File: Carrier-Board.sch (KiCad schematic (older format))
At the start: 45 parts, among them J1 CONN_3-6318491-6, J10 Conn_02x03_Odd_Even, J2 Conn_01x0, J3 Conn_02x26_Odd_Even, J4 SI-51009-F, J5 Conn_02x26_Odd_Even, J6 Conn_01x03_Male, J7 Conn_01x03_Male, J8 Conn_01x06_Male, J9 Conn_02x04_Odd_Even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

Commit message: asdf
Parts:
- removed C1, C3: 10uF, Capacitors_SMD:C_0805, symbol CP
- removed C2, C4: 22uF, Capacitors_SMD:C_0805, symbol CP
- removed D5: D_Zener 9V, Diodes_SMD:D_SOD-323, symbol D_Zener
- removed D6, D7, D8: LED, Diodes_SMD:D_1206, symbol LED
- removed J10: Conn_02x03_Odd_Even, Pin_Headers:Pin_Header_Angled_2x03_Pitch2.54mm, symbol Conn_02x03_Odd_Even
- removed J2: Conn_01x0, Connectors:Barrel_Jack_CUI_PJ-036AH-SMT, symbol Barrel_Jack
- removed J4: SI-51009-F, Carrier-Board:SI-51009-F, symbol Conn_02x09_Odd_Even
- removed J6, J7: Conn_01x03_Male, Pin_Headers:Pin_Header_Angled_1x03_Pitch2.54mm, symbol Conn_01x03_Male
- removed J8: Conn_01x06_Male, Pin_Headers:Pin_Header_Angled_1x06_Pitch2.54mm, symbol Conn_01x06_Male
- removed J9: Conn_02x04_Odd_Even, Pin_Headers:Pin_Header_Angled_2x04_Pitch2.54mm, symbol Conn_02x04_Odd_Even
- removed R1, R5: 160k, Resistors_SMD:R_0805, symbol R
- removed R10, R9: 330, Resistors_SMD:R_0805, symbol R
- removed R11, R12, R13: 10K, Resistors_SMD:R_0603, symbol R
- removed R2: 30.1k, Resistors_SMD:R_0805, symbol R
- removed R23: 330, Resistors_SMD:R_0603, symbol R
- removed R24: 180, Resistors_SMD:R_0603, symbol R
- removed R25: 1k, Resistors_SMD:R_0603, symbol R
- removed R3, R7: 100k, Resistors_SMD:R_0805, symbol R
- removed R4: 63.4k, Resistors_SMD:R_0805, symbol R
- removed R6: 51k, Resistors_SMD:R_0805, symbol R
- removed R8: 56k, Resistors_SMD:R_0805, symbol R
- removed SW1, SW2, SW3: SW_Push, Buttons_Switches_SMD:SW_SPST_B3U-1000P, symbol SW_Push
- removed U1, U2: MPM3620, BusSimulator:QFN-20, symbol MPM3620
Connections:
- net labels removed: +12V, +5V, GNDA, PCE3895CT-ND, PCE3900CT-ND, SPI_POWER
- wire segments 102 -> 24
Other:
- note removed: "12V\n"
- note removed: "3V3\n"
- note removed: "5V SBY\n"
- note removed: "Break out\n"
- note removed: "Ethernet"
- note removed: "GPIO\n"
- note removed: "I2C\n"
- note removed: "LED Indicators\n"
- note removed: "MISC SHIT"
- note removed: "Rs232\n"
- note removed: "SPI\n"
- note removed: "Voltage Supply"

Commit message: stuff
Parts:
- added J2: 0532610671, MOLEX_0532610671, symbol 0532610671
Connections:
- new net: J2.S1 (SHIELD), J2.S2 (SHIELD)
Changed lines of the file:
@@
 LIBS:Carrier-Board
 LIBS:SI-51009-F
+LIBS:0532610271
+LIBS:0532610371
+LIBS:0532610471
+LIBS:0532610671
 LIBS:Carrier-Board-cache
 EELAYER 25 0
@@
 +3.3V
 $Comp
-L GNDREF #PWR022
+L GNDREF #PWR8
 U 1 1 5A0C1B77
 P 3700 8250
-F 0 "#PWR022" H 3700 8000 50  0001 C CNN
+F 0 "#PWR8" H 3700 8000 50  0001 C CNN
 F 1 "GNDREF" H 3700 8100 50  0000 C CNN
 F 2 "" H 3700 8250 50  0001 C CNN
@@
 $EndComp
 $Comp
-L GNDREF #PWR023
+L GNDREF #PWR9
 U 1 1 5A0C1C29
 P 3900 10650
-F 0 "#PWR023" H 3900 10400 50  0001 C CNN
+F 0 "#PWR9" H 3900 10400 50  0001 C CNN
 F 1 "GNDREF" H 3900 10500 50  0000 C CNN
 F 2 "" H 3900 10650 50  0001 C CNN
@@
 $EndComp
 $Comp
-L GNDREF #PWR024
+L GNDREF #PWR12
 U 1 1 5A0C1CDB
 P 4000 9450
-F 0 "#PWR024" H 4000 9200 50  0001 C CNN
+F 0 "#PWR12" H 4000 9200 50  0001 C CNN
 F 1 "GNDREF" H 4000 9300 50  0000 C CNN
 F 2 "" H 4000 9450 50  0001 C CNN
@@
 $EndComp
 $Comp
-L GNDREF #PWR025
+L GNDREF #PWR11
 U 1 1 5A0C1D8D
 P 4000 9050
-F 0 "#PWR025" H 4000 8800 50  0001 C CNN
+F 0 "#PWR11" H 4000 8800 50  0001 C CNN
 F 1 "GNDREF" H 4000 8900 50  0000 C CNN
 F 2 "" H 4000 9050 50  0001 C CNN
@@
 $EndComp
 $Comp
-L GNDREF #PWR026
+L GNDREF #PWR10
 U 1 1 5A0C1E3F
 P 4000 8750
-F 0 "#PWR026" H 4000 8500 50  0001 C CNN
+F 0 "#PWR10" H 4000 8500 50  0001 C CNN
 F 1 "GNDREF" H 4000 8600 50  0000 C CNN
 F 2 "" H 4000 8750 50  0001 C CNN
@@
 $EndComp
 $Comp
-L GNDREF #PWR027
+L GNDREF #PWR13
 U 1 1 5A0C1EF1
 P 4000 9850
-F 0 "#PWR027" H 4000 9600 50  0001 C CNN
+F 0 "#PWR13" H 4000 9600 50  0001 C CNN
 F 1 "GNDREF" H 4000 9700 50  0000 C CNN
 F 2 "" H 4000 9850 50  0001 C CNN
@@
 SATA0_RX-
 $Comp
-L GNDREF #PWR028
+L GNDREF #PWR6
 U 1 1 5A0C49FB
 P 1800 10400
-F 0 "#PWR028" H 1800 10150 50  0001 C CNN
+F 0 "#PWR6" H 1800 10150 50  0001 C CNN
 F 1 "GNDREF" H 1800 10250 50  0000 C CNN
 F 2 "" H 1800 10400 50  0001 C CNN
@@
 $EndComp
 $Comp
-L GNDREF #PWR029
+L GNDREF #PWR7
 U 1 1 5A0C4BAB
 P 1900 10050
-F 0 "#PWR029" H 1900 9800 50  0001 C CNN
+F 0 "#PWR7" H 1900 9800 50  0001 C CNN
 F 1 "GNDREF" H 1900 9900 50  0000 C CNN
 F 2 "" H 1900 10050 50  0001 C CNN
@@
 Sata Connector\n
 $Comp
-L GNDREF #PWR030
+L GNDREF #PWR3
 U 1 1 5A0C6A3D
 P 1450 8950
-F 0 "#PWR030" H 1450 8700 50  0001 C CNN
+F 0 "#PWR3" H 1450 8700 50  0001 C CNN
 F 1 "GNDREF" H 1450 8800 50  0000 C CNN
 F 2 "" H 1450 8950 50  0001 C CNN
@@
 $EndComp
 $Comp
-L GNDREF #PWR031
+L GNDREF #PWR4
 U 1 1 5A0C6D48
 P 1500 9350
-F 0 "#PWR031" H 1500 9100 50  0001 C CNN
+F 0 "#PWR4" H 1500 9100 50  0001 C CNN
 F 1 "GNDREF" H 1500 9200 50  0000 C CNN
 F 2 "" H 1500 9350 50  0001 C CNN
@@
 $EndComp
 $Comp
-L GNDREF #PWR032
+L GNDREF #PWR5
 U 1 1 5A0C77C7
 P 1600 8450
-F 0 "#PWR032" H 1600 8200 50  0001 C CNN
+F 0 "#PWR5" H 1600 8200 50  0001 C CNN
 F 1 "GNDREF" H 1600 8300 50  0000 C CNN
 F 2 "" H 1600 8450 50  0001 C CNN
@@
 $EndComp
 $Comp
-L GNDREF #PWR033
+L GNDREF #PWR1
 U 1 1 5A0DCFAA
 P 750 8350
-F 0 "#PWR033" H 750 8100 50  0001 C CNN
+F 0 "#PWR1" H 750 8100 50  0001 C CNN
 F 1 "GNDREF" H 750 8200 50  0000 C CNN
 F 2 "" H 750 8350 50  0001 C CNN
@@
 $EndComp
 $Comp
-L GNDREF #PWR034
+L GNDREF #PWR2
 U 1 1 5A0DD07C
 P 1100 9050
-F 0 "#PWR034" H 1100 8800 50  0001 C CNN
+F 0 "#PWR2" H 1100 8800 50  0001 C CNN
 F 1 "GNDREF" H 1100 8900 50  0000 C CNN
 F 2 "" H 1100 9050 50  0001 C CNN
@@
 $EndComp
 $Comp
-L GNDREF #PWR035
+L GNDREF #PWR14
 U 1 1 5A0DDC34
 P 4500 8450
-F 0 "#PWR035" H 4500 8200 50  0001 C CNN
+F 0 "#PWR14" H 4500 8200 50  0001 C CNN
 F 1 "GNDREF" H 4500 8300 50  0000 C CNN
 F 2 "" H 4500 8450 50  0001 C CNN
@@
 Wire Bus Line
 	16100 3900 4700 3900
+$Comp
+L 0532610671 J2
+U 1 1 5AB9DE55
+P 2450 1900
+F 0 "J2" H 2250 2331 50  0000 L BNN
+F 1 "0532610671" H 2249 1298 50  0000 L BNN
+F 2 "MOLEX_0532610671" H 2450 1900 50  0001 L BNN
+F 3 "None" H 2450 1900 50  0001 L BNN
+F 4 "Good" H 2450 1900 50  0001 L BNN "Field4"
+F 5 "0532610671" H 2450 1900 50  0001 L BNN "Field5"
+F 6 "1.25mm (.049) Pitch PicoBlade Header, Surface Mount, Right Angle, Lead-free, 6 Circuits" H 2450 1900 50  0001 L BNN "Field6"
+F 7 "0.82 USD" H 2450 1900 50  0001 L BNN "Field7"
+F 8 "Molex" H 2450 1900 50  0001 L BNN "Field8"
+	1    2450 1900
+	1    0    0    -1
+$EndComp
 $EndSCHEMATC

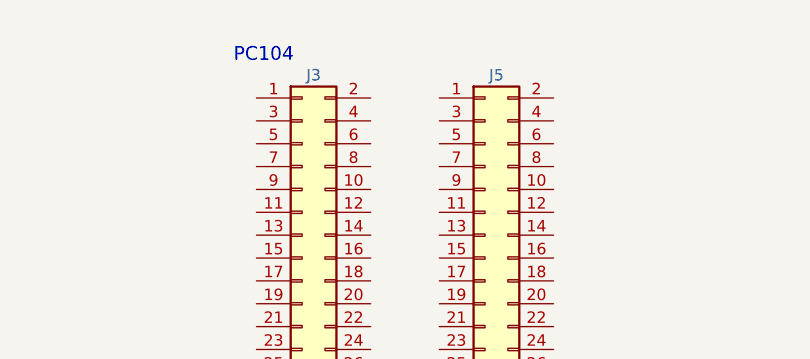
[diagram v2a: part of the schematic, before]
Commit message: Update mCOM connector, correct header refs/silk
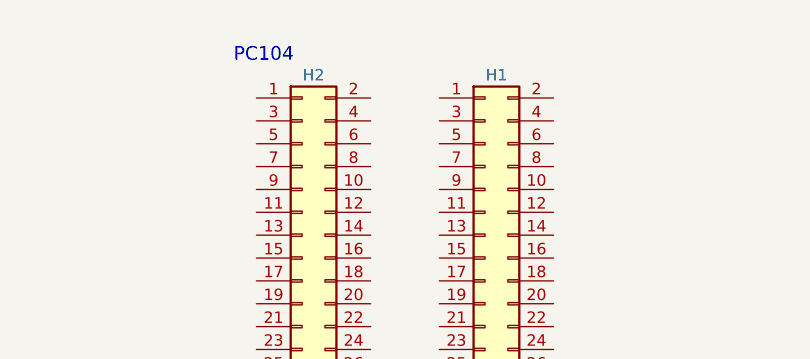
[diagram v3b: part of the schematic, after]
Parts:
- renumbered J5 to H1, J3 to H2
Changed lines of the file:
@@
 LIBS:Carrier-Board
 LIBS:SI-51009-F
+LIBS:MCP6H04-E
+LIBS:BusSimulator
 LIBS:0532610271
 LIBS:0532610371
@@
 $EndComp
 $Comp
-L Conn_02x26_Odd_Even J3
+L Conn_02x26_Odd_Even H2
 U 1 1 5A6C2591
 P 11900 2050
-F 0 "J3" H 11950 3350 50  0000 C CNN
+F 0 "H2" H 11950 3350 50  0000 C CNN
 F 1 "Conn_02x26_Odd_Even" H 11950 650 50  0000 C CNN
 F 2 "Carrier-Board:ESQ-126-XX-X-D" H 11900 2050 50  0001 C CNN
@@
 $EndComp
 $Comp
-L Conn_02x26_Odd_Even J5
+L Conn_02x26_Odd_Even H1
 U 1 1 5A6C25B0
 P 12700 2050
-F 0 "J5" H 12750 3350 50  0000 C CNN
+F 0 "H1" H 12750 3350 50  0000 C CNN
 F 1 "Conn_02x26_Odd_Even" H 12750 650 50  0000 C CNN
 F 2 "Carrier-Board:ESQ-126-XX-X-D" H 12700 2050 50  0001 C CNN

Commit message: SF
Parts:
- H1: value Conn_02x26_Odd_Even -> H1
- H2: value Conn_02x26_Odd_Even -> H2
- J1: value CONN_3-6318491-6 -> s
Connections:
- net CAN_L: now reaches H1.1 (Pin_1)
- net * GPIO PH11: now reaches H1.10 (Pin_10)
- net * ADC1_IN4 (PC4): now reaches H1.13 (Pin_13)
- net * ADC1_IN8 (PC5): now reaches H1.14 (Pin_14)
- net * ADC1_IN5 (PB1): now reaches H1.15 (Pin_15)
- net * ADC1_IN9 (PB0): now reaches H1.16 (Pin_16)
- net * UHF radio UART2_RX / ** UART2_TX: now reaches H1.17 (Pin_17)
- net * UHF radio UART2_TX / ** UART2_RX: now reaches H1.18 (Pin_18)
- net GPS_PPS signal output: now reaches H1.2 (Pin_2)
- net CAN_H: now reaches H1.3 (Pin_3)
- net * I2C3_SDA: now reaches H1.41 (Pin_41)
- net * I2C3_SCL: now reaches H1.43 (Pin_43)
- net 5 V Reaction wheels power supply (default option): now reaches H1.47 (Pin_47)
- net 3.3 V 3C2 board power supply (default option): now reaches H1.48 (Pin_48)
- net *GPIO_PA10: now reaches H1.5 (Pin_5)
- net 3.3V UHF radio power supply (** option 2): now reaches H1.50 (Pin_50)
- net * GPIO_PH6: now reaches H1.7 (Pin_7)
- net * GPIO_PH9: now reaches H1.8 (Pin_8)
- net * GPIO PH10: now reaches H1.9 (Pin_9)
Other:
- note added: "Verify_P10\n"
- moved on the sheet: H1, H2
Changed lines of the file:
@@
 LIBS:Carrier-Board
 LIBS:SI-51009-F
-LIBS:MCP6H04-E
-LIBS:BusSimulator
 LIBS:0532610271
 LIBS:0532610371
@@
 P 9450 4850
 F 0 "J1" H 9800 5100 60  0000 C CNN
-F 1 "CONN_3-6318491-6" H 9800 5450 60  0000 C CNN
+F 1 "CONN_3-6318491-6" H 9800 5450 60  0001 C CNN
 F 2 "BusSimulator:ComExpressMini10" H 9850 2590 60  0001 C CNN
 F 3 "" H 9450 4850 60  0000 C CNN
@@
 P 10950 4850
 F 0 "J1" H 11300 5100 60  0000 C CNN
-F 1 "CONN_3-6318491-6" H 11050 6150 60  0000 C CNN
+F 1 "CONN_3-6318491-6" H 11050 6150 60  0001 C CNN
 F 2 "BusSimulator:ComExpressMini10" H 11350 2590 60  0001 C CNN
 F 3 "" H 10950 4850 60  0000 C CNN
@@
 P 12450 4850
 F 0 "J1" H 12800 5100 60  0000 C CNN
-F 1 "CONN_3-6318491-6" H 13050 6300 60  0000 C CNN
+F 1 "s" H 13050 6300 60  0001 C CNN
 F 2 "BusSimulator:ComExpressMini10" H 12850 2590 60  0001 C CNN
 F 3 "" H 12450 4850 60  0000 C CNN
@@
 P 13950 4850
 F 0 "J1" H 14300 5100 60  0000 C CNN
-F 1 "CONN_3-6318491-6" H 14250 5850 60  0000 C CNN
+F 1 "CONN_3-6318491-6" H 14250 5850 60  0001 C CNN
 F 2 "BusSimulator:ComExpressMini10" H 14350 2590 60  0001 C CNN
 F 3 "" H 13950 4850 60  0000 C CNN
@@
 P 15450 4850
 F 0 "J1" H 15800 5100 60  0000 C CNN
-F 1 "CONN_3-6318491-6" H 15750 5300 60  0000 C CNN
+F 1 "CONN_3-6318491-6" H 15750 5300 60  0001 C CNN
 F 2 "BusSimulator:ComExpressMini10" H 15850 2590 60  0001 C CNN
 F 3 "" H 15450 4850 60  0000 C CNN
@@
 L Conn_02x26_Odd_Even H2
 U 1 1 5A6C2591
-P 11900 2050
-F 0 "H2" H 11950 3350 50  0000 C CNN
-F 1 "Conn_02x26_Odd_Even" H 11950 650 50  0000 C CNN
-F 2 "Carrier-Board:ESQ-126-XX-X-D" H 11900 2050 50  0001 C CNN
-F 3 "" H 11900 2050 50  0001 C CNN
-	1    11900 2050
+P 10200 1850
+F 0 "H2" H 10250 3150 50  0000 C CNN
+F 1 "H2" H 10250 450 50  0000 C CNN
+F 2 "Carrier-Board:ESQ-126-XX-X-D" H 10200 1850 50  0001 C CNN
+F 3 "" H 10200 1850 50  0001 C CNN
+	1    10200 1850
 	1    0    0    -1
 $EndComp
@@
 L Conn_02x26_Odd_Even H1
 U 1 1 5A6C25B0
-P 12700 2050
-F 0 "H1" H 12750 3350 50  0000 C CNN
-F 1 "Conn_02x26_Odd_Even" H 12750 650 50  0000 C CNN
-F 2 "Carrier-Board:ESQ-126-XX-X-D" H 12700 2050 50  0001 C CNN
-F 3 "" H 12700 2050 50  0001 C CNN
-	1    12700 2050
+P 13400 2000
+F 0 "H1" H 13450 3300 50  0000 C CNN
+F 1 "H1" H 13450 600 50  0000 C CNN
+F 2 "Carrier-Board:ESQ-126-XX-X-D" H 13400 2000 50  0001 C CNN
+F 3 "" H 13400 2000 50  0001 C CNN
+	1    13400 2000
 	1    0    0    -1
 $EndComp
@@
 	1    0    0    -1
 $EndComp
+Text GLabel 13200 800  0    60   Input ~ 0
+CAN_L
+Text GLabel 13700 800  2    60   Input ~ 0
+GPS_PPS signal output
+Text GLabel 13200 900  0    60   Input ~ 0
+CAN_H
+Text GLabel 13200 1000 0    60   Input ~ 0
+*GPIO_PA10
+Text GLabel 13200 1100 0    60   Input ~ 0
+* GPIO_PH6
+Text GLabel 13700 1100 2    60   Input ~ 0
+* GPIO_PH9
+Text GLabel 13200 1200 0    60   Input ~ 0
+* GPIO PH10
+Text GLabel 13700 1200 2    60   Input ~ 0
+* GPIO PH11
+Text Notes 14350 1250 0    60   ~ 0
+Verify_P10\n
+Text GLabel 13200 1400 0    60   Input ~ 0
+* ADC1_IN4 (PC4)
+Text GLabel 13700 1400 2    60   Input ~ 0
+* ADC1_IN8 (PC5)
+Text GLabel 13200 1500 0    60   Input ~ 0
+* ADC1_IN5 (PB1)
+Text GLabel 13700 1500 2    60   Input ~ 0
+* ADC1_IN9 (PB0)
+Text GLabel 13200 1600 0    60   Input ~ 0
+* UHF radio UART2_RX / ** UART2_TX
+Text GLabel 13700 1600 2    60   Input ~ 0
+* UHF radio UART2_TX / ** UART2_RX
+Text GLabel 13200 2800 0    60   Input ~ 0
+* I2C3_SDA
+Text GLabel 13200 2900 0    60   Input ~ 0
+* I2C3_SCL
+Text GLabel 13200 3100 0    60   Input ~ 0
+5 V Reaction wheels power supply (default option)
+Text GLabel 13700 3100 2    60   Input ~ 0
+3.3 V 3C2 board power supply (default option)
+Text GLabel 13700 3200 2    60   Input ~ 0
+3.3V UHF radio power supply (** option 2)
 $EndSCHEMATC

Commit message: added connecttos in lib
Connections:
- net SW2_12v: now reaches H2.10 (Pin_10)
- net SW3_BatV: now reaches H2.11 (Pin_11)
- net SW4_BatV: now reaches H2.12 (Pin_12)
- net SW5_5v: now reaches H2.13 (Pin_13)
- net GND: now reaches H2.14 (Pin_14)
- net GND: now also H2.17 (Pin_17), H2.21 (Pin_21), H2.22 (Pin_22), H2.29 (Pin_29), H2.30 (Pin_30), H2.32 (Pin_32), H2.47 (Pin_47), H2.48 (Pin_48), H2.9 (Pin_9)
- net SW6_5v: now reaches H2.15 (Pin_15)
- net SW7_5v: now reaches H2.16 (Pin_16)
- net SW8_3V3: now reaches H2.18 (Pin_18)
- net SW9_3V3: now reaches H2.19 (Pin_19)
- net SW10_3V3: now reaches H2.20 (Pin_20)
- net 12V: now reaches H2.23 (Pin_23)
- net 12V: now also H2.24 (Pin_24)
- net 5V: now reaches H2.25 (Pin_25)
- net 5V: now also H2.26 (Pin_26)
- net 3V3: now reaches H2.27 (Pin_27)
- net 3V3: now also H2.28 (Pin_28)
- net AGND: now reaches H2.31 (Pin_31)
- net DNU: now reaches H2.33 (Pin_33)
- net DNU: now also H2.34 (Pin_34), H2.37 (Pin_37), H2.38 (Pin_38), H2.39 (Pin_39), H2.40 (Pin_40)
- net PCM_IN: now reaches H2.35 (Pin_35)
- net PCM_IN: now also H2.36 (Pin_36)
- net BCR_OUT: now reaches H2.41 (Pin_41)
- net BCR_OUT: now also H2.42 (Pin_42), H2.43 (Pin_43), H2.44 (Pin_44)
- net BatV: now reaches H2.45 (Pin_45)
- net BatV: now also H2.46 (Pin_46)
- net SW1_12v: now reaches H2.8 (Pin_8)
- net 5VUSB_CHG: now reaches H1.32 (Pin_32)
- net 3.3V UHF radio power supply (** option 2): no longer names the net of H1.50 (Pin_50)
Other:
- note added: "3.3 V UHF radio power supply (default option)"
- note added: "NC"
- note added: "Notes:\n\nSW1>PDM1\nSW2>PDM2...\n\nPDM1,PDM2 12V\nPDM3,PDM4 BatV\nPDM5,PDM6,PDM7 5V\nPDM8,PDM9,PDM10 3V3\n"
- note added: "PSU_I2C_CLK"
- note added: "PSU_I2C_DATA\n"
- moved on the sheet: H2
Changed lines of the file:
@@
 L Conn_02x26_Odd_Even H2
 U 1 1 5A6C2591
-P 10200 1850
-F 0 "H2" H 10250 3150 50  0000 C CNN
-F 1 "H2" H 10250 450 50  0000 C CNN
-F 2 "Carrier-Board:ESQ-126-XX-X-D" H 10200 1850 50  0001 C CNN
-F 3 "" H 10200 1850 50  0001 C CNN
-	1    10200 1850
+P 8700 1850
+F 0 "H2" H 8750 3150 50  0000 C CNN
+F 1 "H2" H 8750 450 50  0000 C CNN
+F 2 "Carrier-Board:ESQ-126-XX-X-D" H 8700 1850 50  0001 C CNN
+F 3 "" H 8700 1850 50  0001 C CNN
+	1    8700 1850
 	1    0    0    -1
 $EndComp
@@
 Text GLabel 13700 3100 2    60   Input ~ 0
 3.3 V 3C2 board power supply (default option)
-Text GLabel 13700 3200 2    60   Input ~ 0
-3.3V UHF radio power supply (** option 2)
+Text Notes 16650 3450 0    60   ~ 0
+NC
+Text Notes 16700 3700 0    60   ~ 0
+NC
+Text GLabel 8500 1950 0    60   Input ~ 0
+3V3
+Text GLabel 9000 1950 2    60   Input ~ 0
+3V3
+Text GLabel 8500 2050 0    60   Input ~ 0
+GND
+Text GLabel 9000 2050 2    60   Input ~ 0
+GND
+Text GLabel 8500 2150 0    60   Input ~ 0
+AGND
+Text GLabel 9000 2150 2    60   Input ~ 0
+GND
+Text GLabel 13700 2300 2    60   Input ~ 0
+5VUSB_CHG
+Text Notes 11950 2850 0    60   ~ 0
+PSU_I2C_DATA\n
+Text Notes 11950 2950 0    60   ~ 0
+PSU_I2C_CLK
+Text GLabel 8500 2950 0    60   Input ~ 0
+GND
+Text GLabel 9000 2950 2    60   Input ~ 0
+GND
+Text GLabel 9000 1650 2    60   Input ~ 0
+GND
+Text GLabel 8500 1650 0    60   Input ~ 0
+GND
+Text GLabel 8500 1450 0    60   Input ~ 0
+GND
+Text GLabel 8500 1050 0    60   Input ~ 0
+GND
+Text GLabel 9000 1250 2    60   Input ~ 0
+GND
+Text GLabel 8500 2250 0    60   Input ~ 0
+DNU
+Text GLabel 9000 2250 2    60   Input ~ 0
+DNU
+Text GLabel 8500 2450 0    60   Input ~ 0
+DNU
+Text GLabel 9000 2450 2    60   Input ~ 0
+DNU
+Text GLabel 8500 2550 0    60   Input ~ 0
+DNU
+Text GLabel 9000 2550 2    60   Input ~ 0
+DNU
+Text GLabel 9000 950  2    60   Input ~ 0
+SW1_12v
+Text GLabel 9000 1050 2    60   Input ~ 0
+SW2_12v
+Text GLabel 9000 1150 2    60   Input ~ 0
+SW4_BatV
+Text GLabel 8500 1150 0    60   Input ~ 0
+SW3_BatV
+Text GLabel 8500 1250 0    60   Input ~ 0
+SW5_5v
+Text GLabel 8500 1350 0    60   Input ~ 0
+SW6_5v
+Text GLabel 9000 1350 2    60   Input ~ 0
+SW7_5v
+Text GLabel 9000 1450 2    60   Input ~ 0
+SW8_3V3
+Text GLabel 8500 1550 0    60   Input ~ 0
+SW9_3V3
+Text GLabel 9000 1550 2    60   Input ~ 0
+SW10_3V3
+Text GLabel 8500 1750 0    60   Input ~ 0
+12V
+Text GLabel 9000 1750 2    60   Input ~ 0
+12V
+Text GLabel 8500 1850 0    60   Input ~ 0
+5V
+Text GLabel 9000 1850 2    60   Input ~ 0
+5V
+Text Notes 6100 2000 0    60   ~ 0
+3.3 V UHF radio power supply (default option)
+Text GLabel 8500 2350 0    60   Input ~ 0
+PCM_IN
+Text GLabel 9000 2350 2    60   Input ~ 0
+PCM_IN
+Text GLabel 8500 2650 0    60   Input ~ 0
+BCR_OUT
+Text GLabel 8500 2750 0    60   Input ~ 0
+BCR_OUT
+Text GLabel 9000 2650 2    60   Input ~ 0
+BCR_OUT
+Text GLabel 9000 2750 2    60   Input ~ 0
+BCR_OUT
+Text GLabel 8500 2850 0    60   Input ~ 0
+BatV
+Text GLabel 9000 2850 2    60   Input ~ 0
+BatV
+Text Notes 8300 250  0    60   ~ 0
+Notes:\n\nSW1>PDM1\nSW2>PDM2...\n\nPDM1,PDM2 12V\nPDM3,PDM4 BatV\nPDM5,PDM6,PDM7 5V\nPDM8,PDM9,PDM10 3V3\n
 $EndSCHEMATC

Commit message: ADSFM
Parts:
- added J3: 53261-0771, 53261-0771, symbol 53261-0771
- added J4: 53261-1071, 532611071, symbol 53261-1071
- added P1, P10, P11, P12, P13, P14, P2, P3, P4, P5, P6, P7, P8, P9: 0532610471, MOLEX_0532610471, symbol 0532610471
- J1: value s -> CONN_3-6318491-6
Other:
- moved on the sheet: J2
